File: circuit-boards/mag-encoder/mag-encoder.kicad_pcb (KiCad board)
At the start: 4 copper layers, 19.9 x 27.8 mm, 26 parts, among them J1 CONFIG, J2 0015912055, U1 AP2120N-3.3TRG1, U2 SN74LVC7032ABQAR, U3 MA732GQ

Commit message: Update using Space Cookies sheet template
Signed-off-by: Scott Berman <sgberman1@gmail.com>
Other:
- board text added: "WCP-1971 2025 1868 SPACE COOKIES"
- board text removed: "3V3"
- board text removed: "CS"
- board text removed: "GND"
- board text removed: "MISO"
- board text removed: "MOSI"
- board text removed: "SCLK"
- board text removed: "WCP-1971 2025"

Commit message: Update silk to new part number
Signed-off-by: Scott Berman <sgberman1@gmail.com>
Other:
- board text added: "WCP MAG ENCODER V1"
- board text added: "WCP-2435 2025 1868 SPACE COOKIES"
- board text removed: "MAG ENCODER V1"
- board text removed: "WCP-1971 2025 1868 SPACE COOKIES"

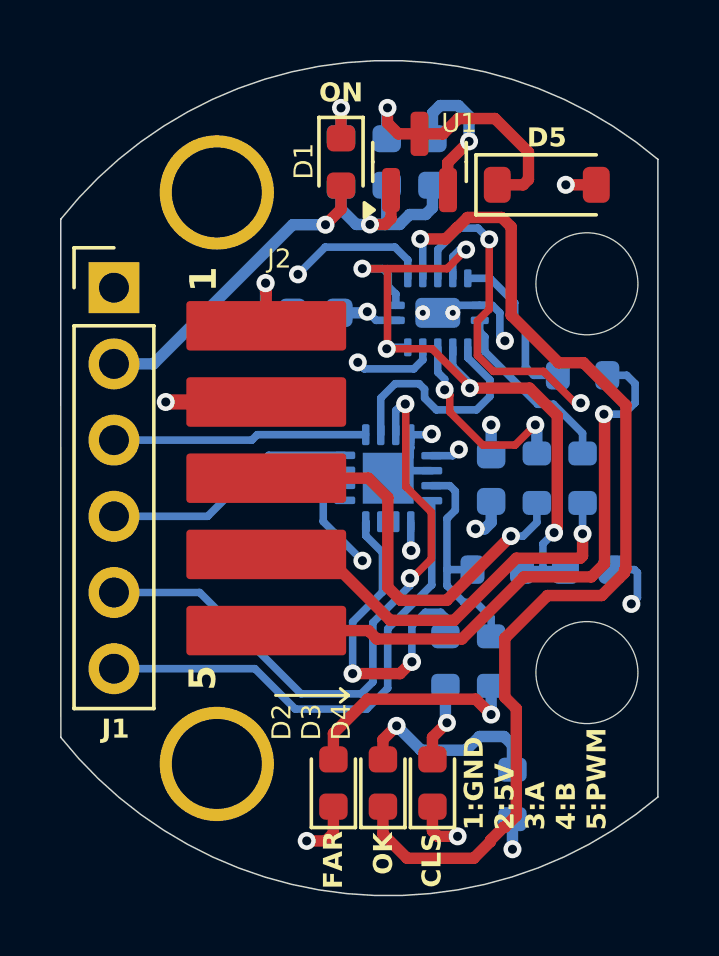
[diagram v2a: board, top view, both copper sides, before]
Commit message: Add open source license to mag encoder.
Signed-off-by: Scott Berman <sgberman1@gmail.com>
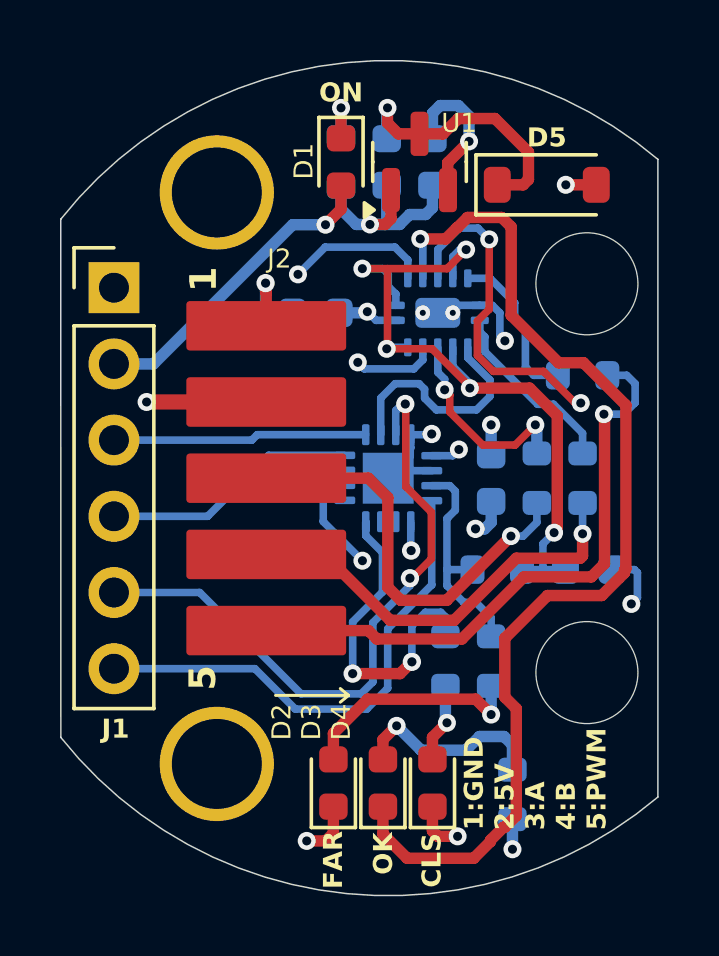
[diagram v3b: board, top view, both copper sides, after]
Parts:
- C1, C2, C3, C4, C5: footprint Capacitor_SMD:C_0603_1608Metric -> mag-encoder:C_0603_1608Metric
- D1, D2, D3, D4: footprint LED_SMD:LED_0603_1608Metric -> mag-encoder:LED_0603_1608Metric
- D5: footprint Diode_SMD:D_SOD-123 -> mag-encoder:D_SOD-123
- G***: footprint Logos:WCP-Logo_200 -> mag-encoder:WCP-Logo_200
- J1: footprint Connector_PinHeader_2.54mm:PinHeader_1x06_P2.54mm_Vertical -> mag-encoder:PinHeader_1x06_P2.54mm_Vertical
- R1, R2, R3, R4, R5, R6, R7, R8: footprint Resistor_SMD:R_0603_1608Metric -> mag-encoder:R_0603_1608Metric
- U1: footprint Package_TO_SOT_SMD:SOT-23 -> mag-encoder:SOT-23
- moved G*** 5.71 mm to (227.7, 129.4)
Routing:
- net +5V_IN: track 4.36 -> 5.00 mm
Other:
- board text added: "NOTES: 1. LAYERS: 4 2. PCB THICKNESS: 1.6mm 3. PCB COLOR: BLUE 4. SILKSCREEN: WHITE 5. MATERIAL TYPE: FR4 TG135 6. SURFACE FINISH: ENIG 7. OUTER COPPER WEIGHT: 1oz 8. INNER COPPER WEIGHT: 0.5oz 9. IMPEDANCE CONTROL: NO 10. VIA COVERING: PLUGGED 11. MIN VIA HOLE DIA: 0.2mm 12. BOARD OUTLINE TOLERANCE: +/-0.2mm"
- board text added: "WCP MAG ENCODER V1 (C)2025 1868 SPACE COOKIES WCP-2435"
- board text removed: "NOTES: 1. LAYERS: 4 2. PCB THICKNESS: 1.6mm 3. PCB COLOR: BLUE 4. SILKSCREEN: WHITE 5. MATERIAL TYPE: FR4 TG-155 6. SURFACE FINISH: ENIG 7. OUTER COPPER WEIGHT: 1oz 8. INNER COPPER WEIGHT: 0.5oz 9. IMPEDANCE CONTROL: NO 10. VIA COVERING: PLUGGED 11. MIN VIA HOLE DIA: 0.2mm 12. BOARD OUTLINE TOLERANCE: +/-0.2mm"
- board text removed: "WCP MAG ENCODER V1"
- board text removed: "WCP-2435 2025 1868 SPACE COOKIES"
